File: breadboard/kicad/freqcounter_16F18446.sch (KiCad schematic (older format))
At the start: 11 parts, among them J1 ICSP PICKIT, J2 USB-Serial, P1 LCD_DISPLAY_16X2, U1 PIC16F18446, Y1 Crystal 8MHz

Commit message: Updated kicad schematic
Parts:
- added R1: 10k, Resistor_SMD:R_0805_2012Metric_Pad1.15x1.40mm_HandSolder, symbol Device:R
- added R5: 180, Resistor_SMD:R_0805_2012Metric_Pad1.15x1.40mm_HandSolder, symbol Device:R
- renumbered C5 to C1, C1 to C2, R11 to R2, R12 to R3, R1 to R4
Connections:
- net GND: now also R5.2; no longer P1.16 (P16), P1.3 (P3)
- net INPUT_ZCD: now also R1.1; no longer U1.17 (RA2)
- new net: R1.2, U1.17 (RA2)
- new net: P1.3 (P3), R5.1
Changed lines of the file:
@@
 $EndComp
 $Comp
-L Device:C C5
+L Device:C C1
 U 1 1 5E6A67BE
 P 5000 2000
-F 0 "C5" V 4950 2050 50  0000 L CNN
+F 0 "C1" V 4950 2050 50  0000 L CNN
 F 1 "100nF" V 4850 1900 50  0000 L CNN
 F 2 "Capacitor_SMD:C_0805_2012Metric_Pad1.15x1.40mm_HandSolder" H 5038 1850 50  0001 C CNN
@@
 $EndComp
 $Comp
-L Device:R R1
+L Device:R R4
 U 1 1 5E71FB56
 P 3650 3200
-F 0 "R1" V 3750 3150 50  0000 L CNN
+F 0 "R4" V 3750 3150 50  0000 L CNN
 F 1 "1K" V 3650 3150 50  0000 L CNN
 F 2 "Resistor_SMD:R_0805_2012Metric_Pad1.15x1.40mm_HandSolder" V 3580 3200 50  0001 C CNN
@@
 $EndComp
 $Comp
-L Device:C C1
+L Device:C C2
 U 1 1 5E71FBD7
 P 2850 3200
-F 0 "C1" V 2700 3150 50  0000 L CNN
+F 0 "C2" V 2700 3150 50  0000 L CNN
 F 1 "2.2nF" V 2600 3150 50  0000 L CNN
 F 2 "Capacitor_SMD:C_0805_2012Metric_Pad1.15x1.40mm_HandSolder" H 2888 3050 50  0001 C CNN
@@
 	0    1    -1   0
 $EndComp
-Text GLabel 6900 2700 2    40   Input ~ 0
+Text GLabel 7100 2700 2    40   Input ~ 0
 INPUT_ZCD
 $Comp
@@
 $EndComp
 $Comp
-L Device:R R11
+L Device:R R2
 U 1 1 5E8D7C95
 P 5750 2800
-F 0 "R11" V 5700 2950 50  0000 L CNN
+F 0 "R2" V 5700 2950 50  0000 L CNN
 F 1 "180" V 5745 2725 50  0000 L CNN
 F 2 "Resistor_SMD:R_0805_2012Metric_Pad1.15x1.40mm_HandSolder" V 5680 2800 50  0001 C CNN
@@
 $EndComp
 $Comp
-L Device:R R12
+L Device:R R3
 U 1 1 5E8DA958
 P 5750 2900
-F 0 "R12" V 5700 3050 50  0000 L CNN
+F 0 "R3" V 5700 3050 50  0000 L CNN
 F 1 "180" V 5745 2825 50  0000 L CNN
 F 2 "Resistor_SMD:R_0805_2012Metric_Pad1.15x1.40mm_HandSolder" V 5680 2900 50  0001 C CNN
@@
 Text GLabel 5500 2600 2    40   Input ~ 0
 ICSPCLK
-Wire Wire Line
-	5500 2700 6900 2700
 $Comp
 L LCD_DISPLAY_16X2:LCD_DISPLAY_16X2 P1
@@
 	5100 4100 5100 4400
 Connection ~ 5000 4100
-Text GLabel 4600 4000 1    40   Input ~ 0
-GND
-Wire Wire Line
-	4600 4100 4600 4000
+Text GLabel 4100 4100 0    40   Input ~ 0
+GND
 Connection ~ 4600 4100
-Wire Wire Line
-	4600 4100 4400 4100
-Wire Wire Line
-	4400 4100 4400 4400
-Wire Wire Line
-	5100 4100 5700 4100
-Wire Wire Line
-	5700 4100 5700 4400
-Connection ~ 5100 4100
 Text GLabel 5500 3200 2    40   Input ~ 0
 LCD_D4
@@
 LCD_D6
 Wire Wire Line
-	4400 4100 4200 4100
-Wire Wire Line
 	4200 4100 4200 4400
-Connection ~ 4400 4100
 Text GLabel 4300 4400 1    40   Input ~ 0
 VDD
@@
 Wire Wire Line
 	4050 2500 4500 2500
+$Comp
+L Device:R R1
+U 1 1 5EA419F2
+P 6950 2700
+F 0 "R1" V 6850 2650 50  0000 L CNN
+F 1 "10k" V 6945 2625 50  0000 L CNN
+F 2 "Resistor_SMD:R_0805_2012Metric_Pad1.15x1.40mm_HandSolder" V 6880 2700 50  0001 C CNN
+F 3 "~" H 6950 2700 50  0001 C CNN
+	1    6950 2700
+	0    1    1    0
+$EndComp
+Wire Wire Line
+	5500 2700 6800 2700
+Wire Wire Line
+	4200 4100 4600 4100
+$Comp
+L Device:R R5
+U 1 1 5EA4312D
+P 4550 3900
+F 0 "R5" V 4600 3650 50  0000 L CNN
+F 1 "180" V 4545 3825 50  0000 L CNN
+F 2 "Resistor_SMD:R_0805_2012Metric_Pad1.15x1.40mm_HandSolder" V 4480 3900 50  0001 C CNN
+F 3 "~" H 4550 3900 50  0001 C CNN
+	1    4550 3900
+	0    -1   -1   0
+$EndComp
+Wire Wire Line
+	4100 4100 4200 4100
+Connection ~ 4200 4100
+Wire Wire Line
+	4400 3900 4400 4400
+Wire Wire Line
+	4700 3900 5100 3900
+Wire Wire Line
+	5100 3900 5100 4100
+Connection ~ 5100 4100
 $EndSCHEMATC

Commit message: Updated kicad schematic
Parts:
- R5: value 180 -> 1k
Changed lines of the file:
@@
 P 4550 3900
 F 0 "R5" V 4600 3650 50  0000 L CNN
-F 1 "180" V 4545 3825 50  0000 L CNN
+F 1 "1k" V 4545 3825 50  0000 L CNN
 F 2 "Resistor_SMD:R_0805_2012Metric_Pad1.15x1.40mm_HandSolder" V 4480 3900 50  0001 C CNN
 F 3 "~" H 4550 3900 50  0001 C CNN

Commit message: Bugfix schematic and PCB
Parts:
- R5: value 1k -> 2k2
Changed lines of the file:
@@
 P 4550 3900
 F 0 "R5" V 4600 3650 50  0000 L CNN
-F 1 "1k" V 4545 3825 50  0000 L CNN
+F 1 "2k2" V 4545 3825 50  0000 L CNN
 F 2 "Resistor_SMD:R_0805_2012Metric_Pad1.15x1.40mm_HandSolder" V 4480 3900 50  0001 C CNN
 F 3 "~" H 4550 3900 50  0001 C CNN

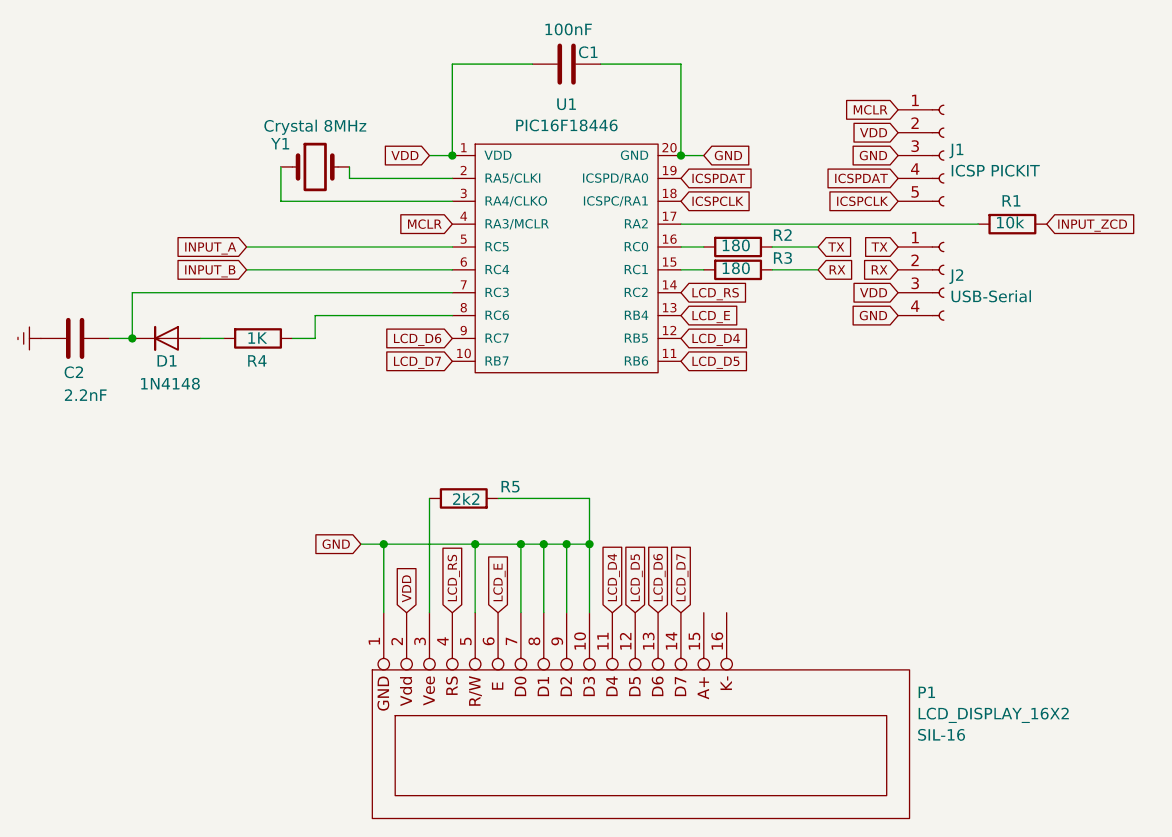
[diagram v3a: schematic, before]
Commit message: Updated project. Changed UART and LCD pins
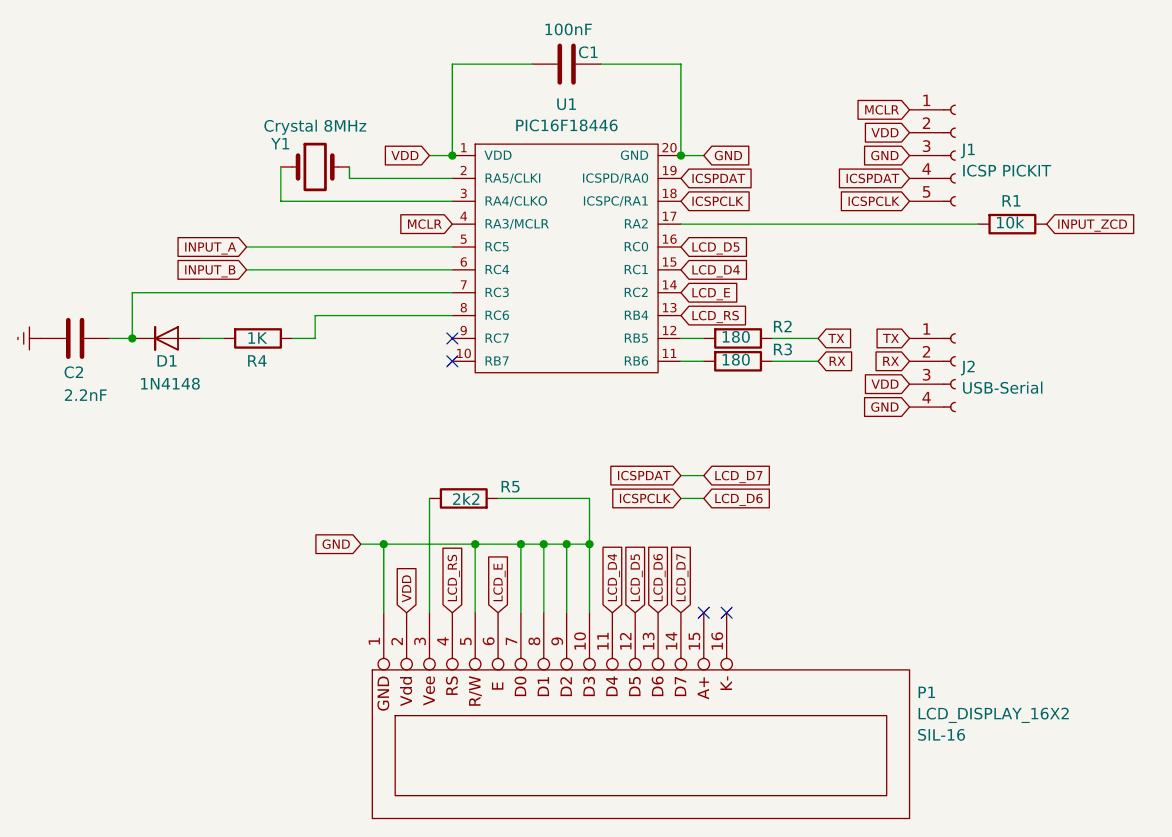
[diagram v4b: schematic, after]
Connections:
- net ICSPCLK: now also P1.13 (P13)
- net ICSPDAT: now also P1.14 (P14)
- net LCD_D4: now also U1.15 (RC1); no longer U1.12 (RB5)
- net LCD_D5: now also U1.16 (RC0); no longer U1.11 (RB6)
- net LCD_E: now also U1.14 (RC2); no longer U1.13 (RB4)
- net LCD_RS: now also U1.13 (RB4); no longer U1.14 (RC2)
- net at R3.2: now also U1.11 (RB6); no longer U1.15 (RC1)
- net at R2.2: now also U1.12 (RB5); no longer U1.16 (RC0)
- net LCD_D6: no longer names the net of U1.9 (RC7)
- net LCD_D6: no longer P1.13 (P13)
- net LCD_D7: no longer names the net of U1.10 (RB7)
- net LCD_D7: no longer P1.14 (P14)
- no-connect marks 0 -> 4
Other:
- moved on the sheet: J1, J2, R2, R3
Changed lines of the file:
@@
 	1    0    0    -1
 $EndComp
-Text GLabel 6450 2200 0    40   Input ~ 0
+Text GLabel 6500 2200 0    40   Input ~ 0
 MCLR
-Text GLabel 6450 2300 0    40   Input ~ 0
+Text GLabel 6500 2300 0    40   Input ~ 0
 VDD
-Text GLabel 6450 2400 0    40   Input ~ 0
+Text GLabel 6500 2400 0    40   Input ~ 0
 GND
 Text GLabel 3600 2800 0    40   Input ~ 0
@@
 L Device:R R2
 U 1 1 5E8D7C95
-P 5750 2800
-F 0 "R2" V 5700 2950 50  0000 L CNN
-F 1 "180" V 5745 2725 50  0000 L CNN
-F 2 "Resistor_SMD:R_0805_2012Metric_Pad1.15x1.40mm_HandSolder" V 5680 2800 50  0001 C CNN
-F 3 "~" H 5750 2800 50  0001 C CNN
-	1    5750 2800
+P 5750 3200
+F 0 "R2" V 5700 3350 50  0000 L CNN
+F 1 "180" V 5745 3125 50  0000 L CNN
+F 2 "Resistor_SMD:R_0805_2012Metric_Pad1.15x1.40mm_HandSolder" V 5680 3200 50  0001 C CNN
+F 3 "~" H 5750 3200 50  0001 C CNN
+	1    5750 3200
 	0    1    1    0
 $EndComp
@@
 L Device:R R3
 U 1 1 5E8DA958
-P 5750 2900
-F 0 "R3" V 5700 3050 50  0000 L CNN
-F 1 "180" V 5745 2825 50  0000 L CNN
-F 2 "Resistor_SMD:R_0805_2012Metric_Pad1.15x1.40mm_HandSolder" V 5680 2900 50  0001 C CNN
-F 3 "~" H 5750 2900 50  0001 C CNN
-	1    5750 2900
+P 5750 3300
+F 0 "R3" V 5700 3450 50  0000 L CNN
+F 1 "180" V 5745 3225 50  0000 L CNN
+F 2 "Resistor_SMD:R_0805_2012Metric_Pad1.15x1.40mm_HandSolder" V 5680 3300 50  0001 C CNN
+F 3 "~" H 5750 3300 50  0001 C CNN
+	1    5750 3300
 	0    1    1    0
 $EndComp
@@
 L Connector:Conn_01x04_Female J2
 U 1 1 5EA1E8B8
-P 6650 2900
-F 0 "J2" H 6678 2875 50  0000 L CNN
-F 1 "USB-Serial" H 6678 2782 50  0000 L CNN
-F 2 "" H 6650 2900 50  0001 C CNN
-F 3 "~" H 6650 2900 50  0001 C CNN
-	1    6650 2900
+P 6700 3300
+F 0 "J2" H 6728 3275 50  0000 L CNN
+F 1 "USB-Serial" H 6728 3182 50  0000 L CNN
+F 2 "" H 6700 3300 50  0001 C CNN
+F 3 "~" H 6700 3300 50  0001 C CNN
+	1    6700 3300
 	1    0    0    -1
 $EndComp
 Text GLabel 5600 2400 2    40   Input ~ 0
 GND
-Text GLabel 6450 3100 0    40   Input ~ 0
-GND
-Text GLabel 6450 3000 0    40   Input ~ 0
+Text GLabel 6500 3500 0    40   Input ~ 0
+GND
+Text GLabel 6500 3400 0    40   Input ~ 0
 VDD
 $Comp
 L Connector:Conn_01x05_Female J1
 U 1 1 5EA272A8
-P 6650 2400
-F 0 "J1" H 6678 2425 50  0000 L CNN
-F 1 "ICSP PICKIT" H 6678 2332 50  0000 L CNN
-F 2 "" H 6650 2400 50  0001 C CNN
-F 3 "~" H 6650 2400 50  0001 C CNN
-	1    6650 2400
+P 6700 2400
+F 0 "J1" H 6728 2425 50  0000 L CNN
+F 1 "ICSP PICKIT" H 6728 2332 50  0000 L CNN
+F 2 "" H 6700 2400 50  0001 C CNN
+F 3 "~" H 6700 2400 50  0001 C CNN
+	1    6700 2400
 	1    0    0    -1
 $EndComp
@@
 	4500 2900 3600 2900
 Wire Wire Line
-	5500 2800 5600 2800
-Wire Wire Line
-	5500 2900 5600 2900
-Text GLabel 6100 2800 2    40   Input ~ 0
+	5500 3200 5600 3200
+Wire Wire Line
+	5500 3300 5600 3300
+Text GLabel 6100 3200 2    40   Input ~ 0
 TX
 Wire Wire Line
-	6100 2800 5900 2800
-Text GLabel 6100 2900 2    40   Input ~ 0
+	6100 3200 5900 3200
+Text GLabel 6100 3300 2    40   Input ~ 0
 RX
 Wire Wire Line
-	6100 2900 5900 2900
-Text GLabel 6450 2800 0    40   Input ~ 0
+	6100 3300 5900 3300
+Text GLabel 6500 3200 0    40   Input ~ 0
 TX
-Text GLabel 6450 2900 0    40   Input ~ 0
+Text GLabel 6500 3300 0    40   Input ~ 0
 RX
-Text GLabel 6450 2500 0    40   Input ~ 0
+Text GLabel 6500 2500 0    40   Input ~ 0
 ICSPDAT
-Text GLabel 6450 2600 0    40   Input ~ 0
+Text GLabel 6500 2600 0    40   Input ~ 0
 ICSPCLK
 Text GLabel 5500 2500 2    40   Input ~ 0
@@
 	1    0    0    -1
 $EndComp
+Text GLabel 5500 3100 2    40   Input ~ 0
+LCD_RS
 Text GLabel 5500 3000 2    40   Input ~ 0
-LCD_RS
-Text GLabel 5500 3100 2    40   Input ~ 0
 LCD_E
 Text GLabel 4700 4400 1    40   Input ~ 0
@@
 GND
 Connection ~ 4600 4100
-Text GLabel 5500 3200 2    40   Input ~ 0
+Text GLabel 5500 2900 2    40   Input ~ 0
 LCD_D4
-Text GLabel 5500 3300 2    40   Input ~ 0
+Text GLabel 5500 2800 2    40   Input ~ 0
 LCD_D5
-Text GLabel 4500 3300 0    40   Input ~ 0
+Text GLabel 5600 3800 2    40   Input ~ 0
 LCD_D7
-Text GLabel 4500 3200 0    40   Input ~ 0
+Text GLabel 5600 3900 2    40   Input ~ 0
 LCD_D6
 Text GLabel 5200 4400 1    40   Input ~ 0
@@
 	5100 3900 5100 4100
 Connection ~ 5100 4100
+Text GLabel 5500 3800 0    40   Input ~ 0
+ICSPDAT
+Text GLabel 5500 3900 0    40   Input ~ 0
+ICSPCLK
+Wire Wire Line
+	5500 3800 5600 3800
+Wire Wire Line
+	5600 3900 5500 3900
+NoConn ~ 4500 3300
+NoConn ~ 4500 3200
+NoConn ~ 5700 4400
+NoConn ~ 5600 4400
 $EndSCHEMATC
